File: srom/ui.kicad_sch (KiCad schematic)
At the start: 10 parts, among them J302 Conn_01x04_Female, J303 Conn_01x03_Female, J304 Conn_01x06_Female, SW301 SW_MEC_5E, SW302 RotaryEncoder_Switch, SW303 SW_MEC_5E, U301 Pico-3 UI

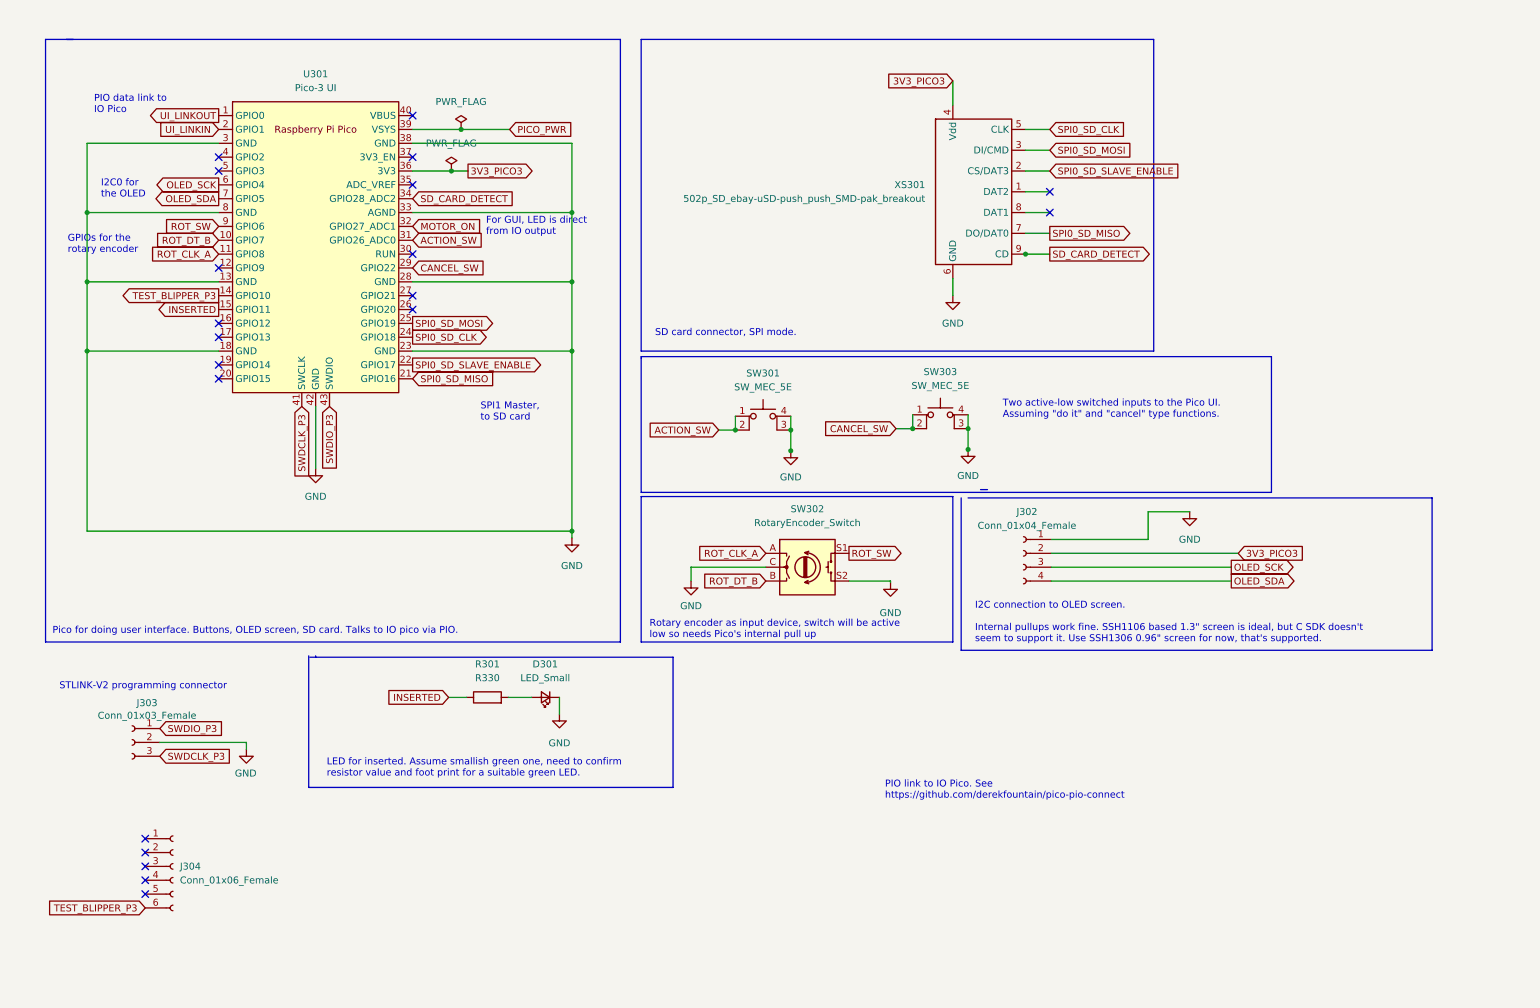
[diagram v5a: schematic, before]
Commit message: add rear edge schematic, RUN switch, ROMCS2 signal
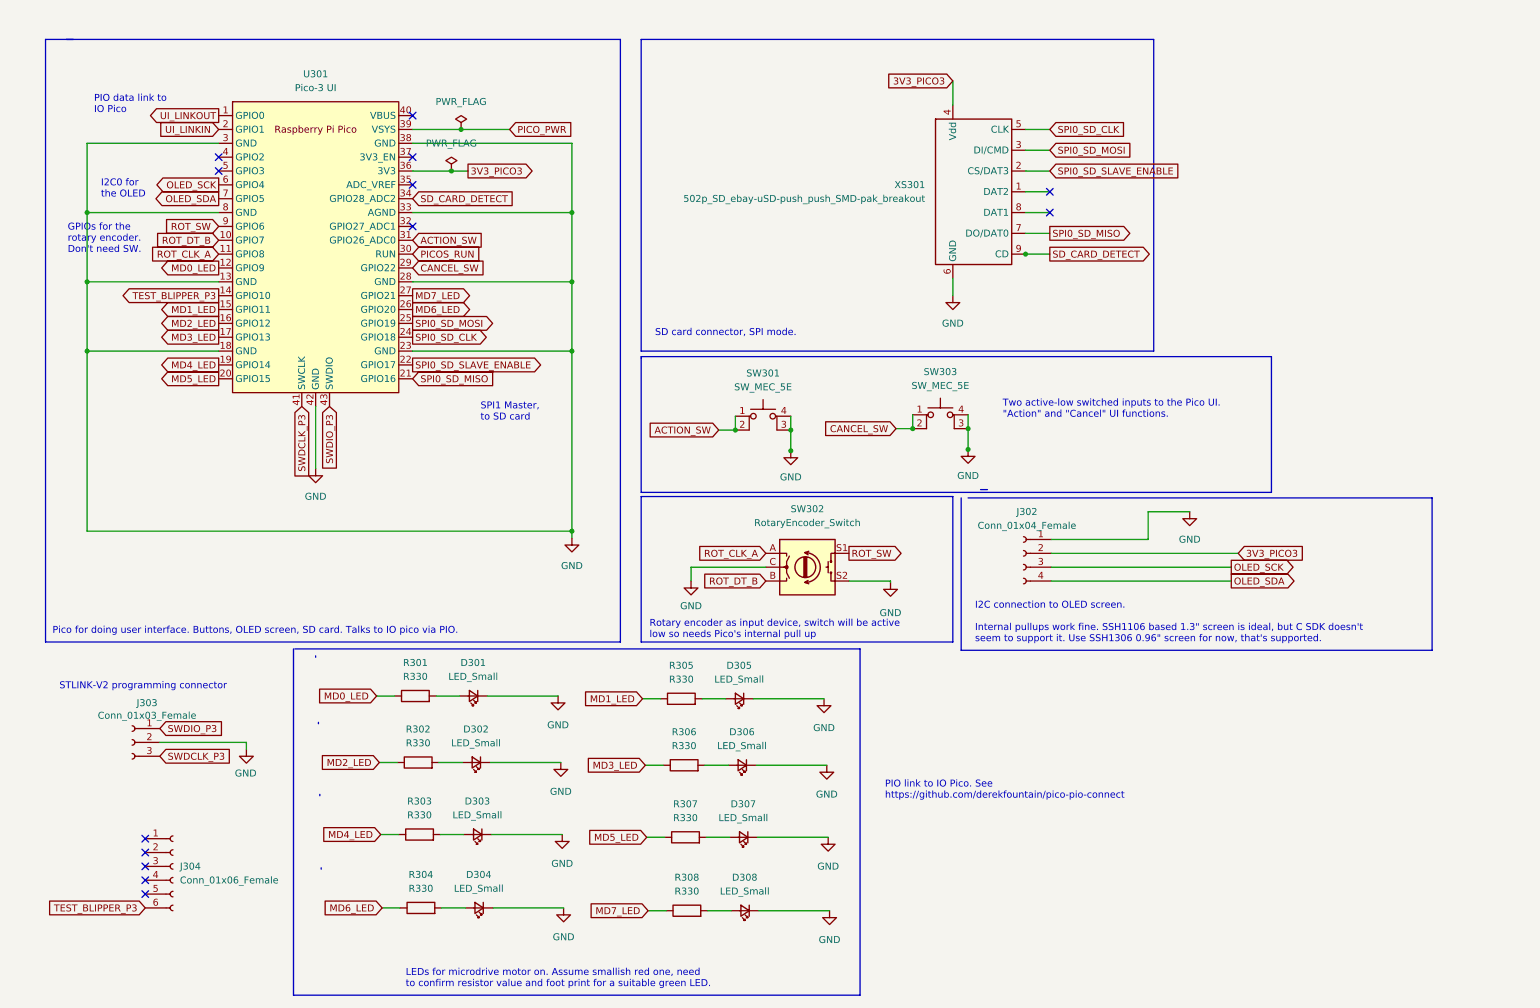
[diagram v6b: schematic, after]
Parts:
- added D302, D303, D304, D305, D306, D307, D308: LED_Small, LED_THT:LED_D3.0mm, symbol Device:LED_Small
- added R302, R303, R304, R305, R306, R307, R308: R330, Resistor_SMD:R_1206_3216Metric_Pad1.30x1.75mm_HandSolder, symbol Device:R
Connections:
- net GND: now also D302.1 (K), D303.1 (K), D304.1 (K), D305.1 (K), D306.1 (K), D307.1 (K), D308.1 (K)
- net MD0_LED: now reaches U301.12 (GPIO9)
- net MD0_LED: now also R301.1
- net MD2_LED: now reaches U301.16 (GPIO12)
- net MD2_LED: now also R302.1
- net MD3_LED: now reaches U301.17 (GPIO13)
- net MD3_LED: now also R306.1
- net MD4_LED: now reaches U301.19 (GPIO14)
- net MD4_LED: now also R303.1
- net MD5_LED: now reaches U301.20 (GPIO15)
- net MD5_LED: now also R307.1
- net MD6_LED: now reaches U301.26 (GPIO20)
- net MD6_LED: now also R304.1
- net MD7_LED: now reaches U301.27 (GPIO21)
- net MD7_LED: now also R308.1
- net PICOS_RUN: now reaches U301.30 (RUN)
- net INSERTED renamed MD1_LED
- net MD1_LED: now also R305.1; no longer R301.1
- net MOTOR_ON: no longer names the net of U301.32 (GPIO27_ADC1)
- new net: D304.2 (A), R304.2
- new net: D302.2 (A), R302.2
- new net: D308.2 (A), R308.2
- new net: D305.2 (A), R305.2
- new net: D303.2 (A), R303.2
- new net: D306.2 (A), R306.2
- new net: D307.2 (A), R307.2
- no-connect marks 20 -> 13
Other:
- note added: "GPIOs for the rotary encoder. Don't need SW."
- note added: "LEDs for microdrive motor on. Assume smallish red one, need to confirm resistor value and foot print for a suitable green LED."
- note added: "Two active-low switched inputs to the Pico UI. "Action" and "Cancel" UI functions."
- note removed: "For GUI, LED is direct from IO output"
- note removed: "GPIOs for the rotary encoder"
- note removed: "LED for inserted. Assume smallish green one, need to confirm resistor value and foot print for a suitable green LED."
- note removed: "Two active-low switched inputs to the Pico UI. Assuming "do it" and "cancel" type functions."
- moved on the sheet: D301, R301

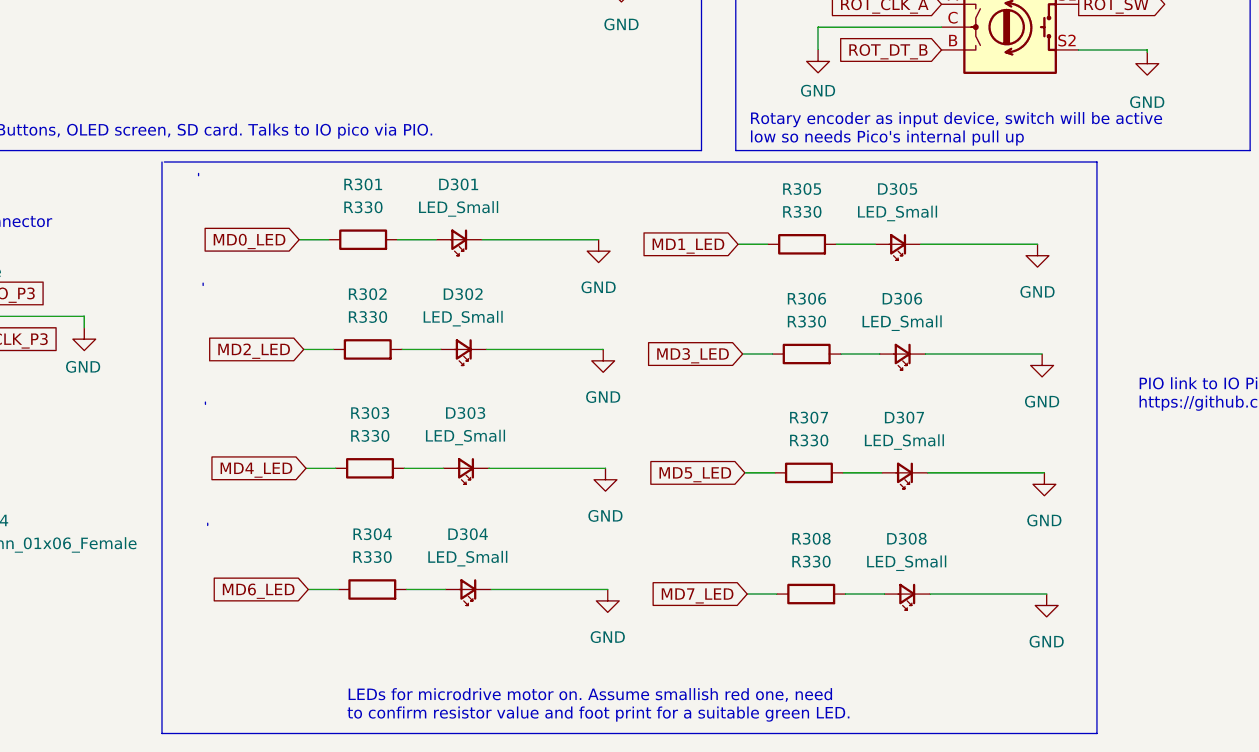
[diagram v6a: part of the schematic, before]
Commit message: 8 LEDs on UI Pico's GPIOs, 2 tested and working
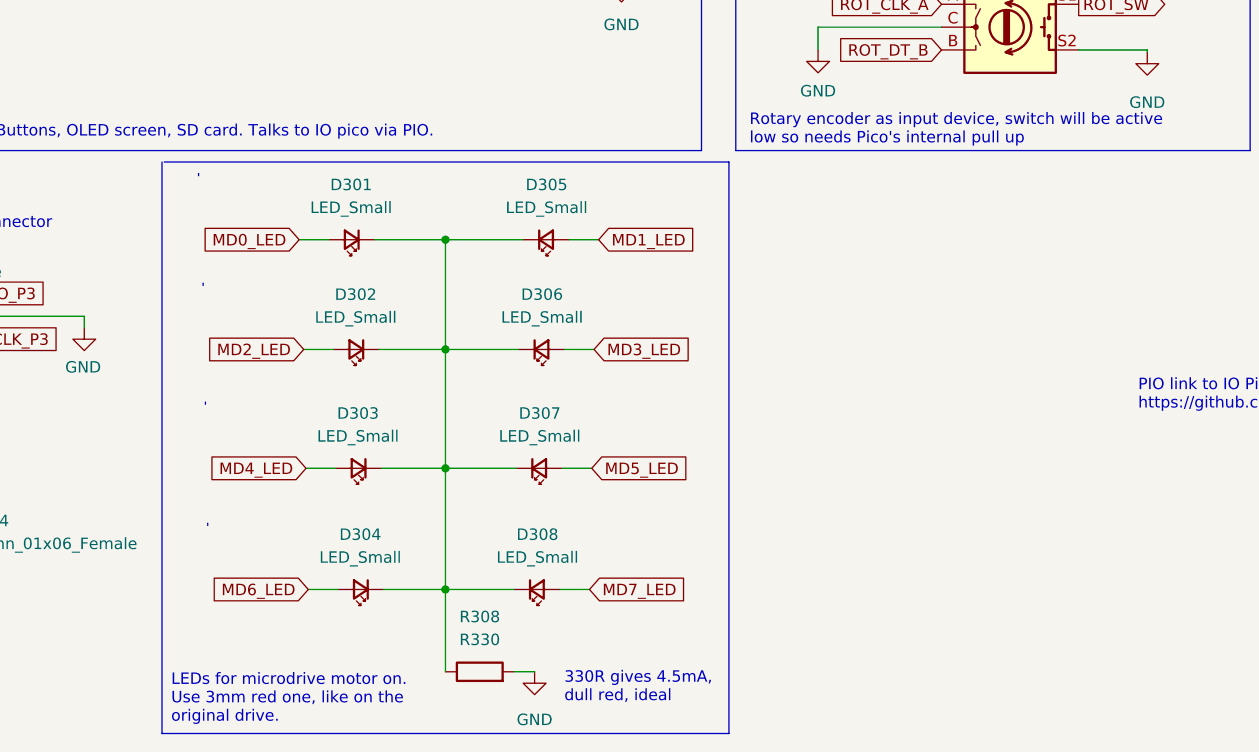
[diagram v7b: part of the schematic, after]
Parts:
- removed R301, R302, R303, R304, R305, R306, R307: R330, Resistor_SMD:R_1206_3216Metric_Pad1.30x1.75mm_HandSolder, symbol Device:R
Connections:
- net GND: now also R308.2; no longer D301.1 (K), D302.1 (K), D303.1 (K), D304.1 (K), D305.1 (K), D306.1 (K), D307.1 (K), D308.1 (K)
- net MD0_LED: now also D301.2 (A)
- net MD1_LED: now also D305.2 (A)
- net MD2_LED: now also D302.2 (A)
- net MD3_LED: now also D306.2 (A)
- net MD4_LED: now also D303.2 (A)
- net MD5_LED: now also D307.2 (A)
- net MD6_LED: now also D304.2 (A)
- net MD7_LED: now also D308.2 (A); no longer R308.1
- new net: D301.1 (K), D302.1 (K), D303.1 (K), D304.1 (K), D305.1 (K), D306.1 (K), D307.1 (K), D308.1 (K), R308.1
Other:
- note added: "330R gives 4.5mA, dull red, ideal"
- note added: "LEDs for microdrive motor on. Use 3mm red one, like on the original drive."
- note removed: "LEDs for microdrive motor on. Assume smallish red one, need to confirm resistor value and foot print for a suitable green LED."
- moved on the sheet: D301, D302, D303, D304, D305, D306, D307, D308, R308

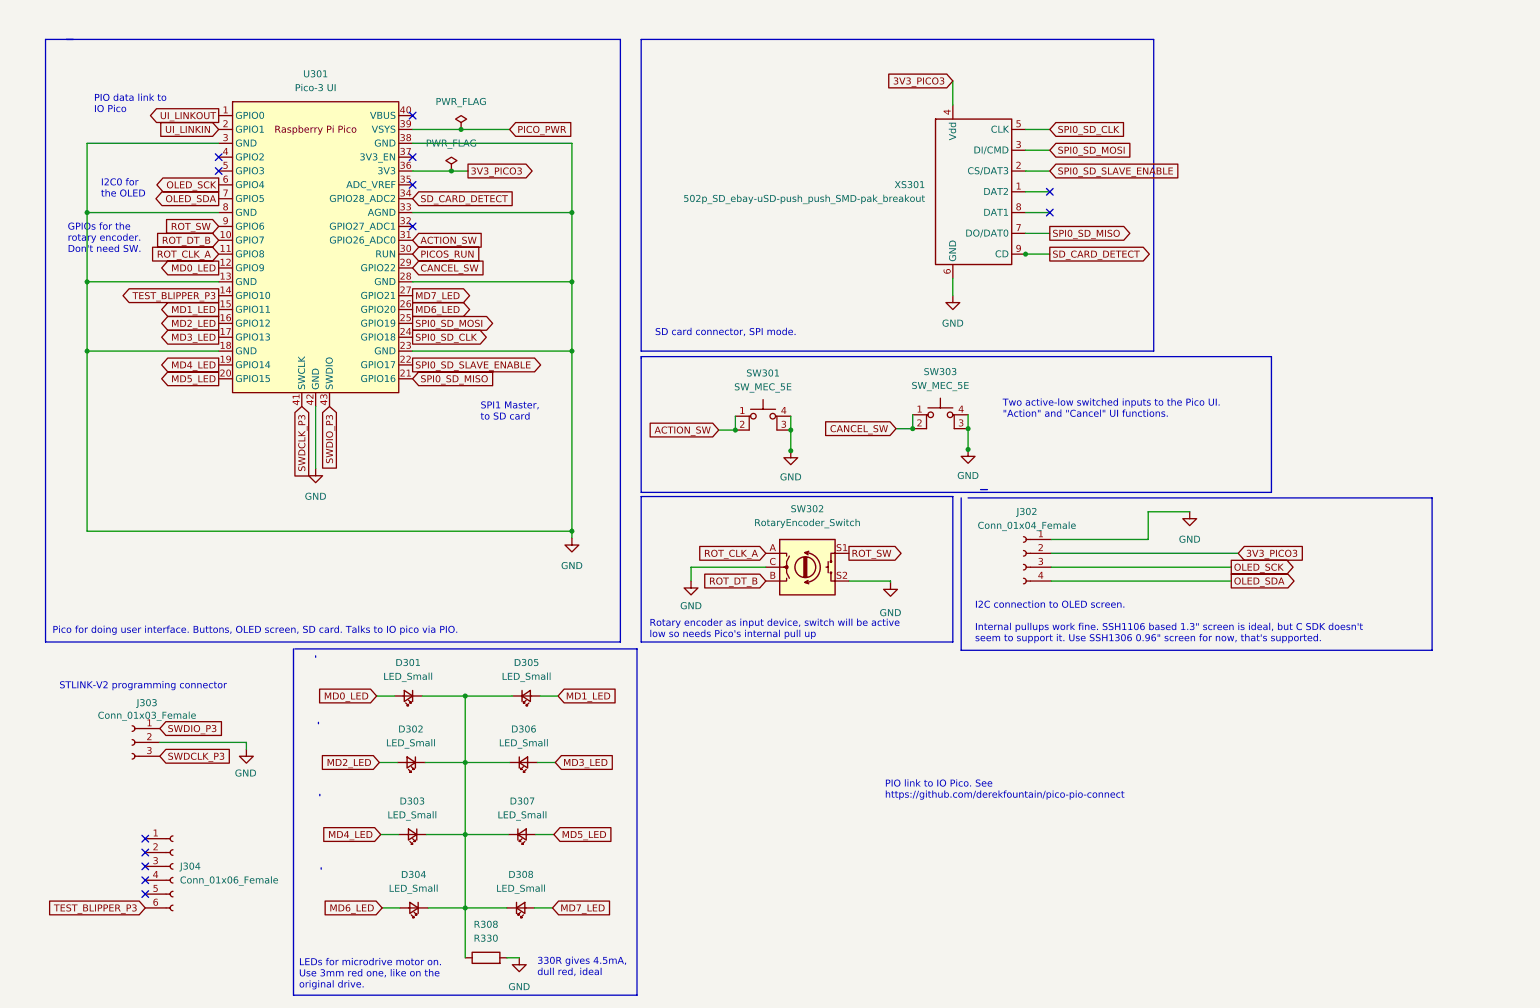
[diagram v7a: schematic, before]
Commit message: remove test point connectors, no needed on next board (famous last words)
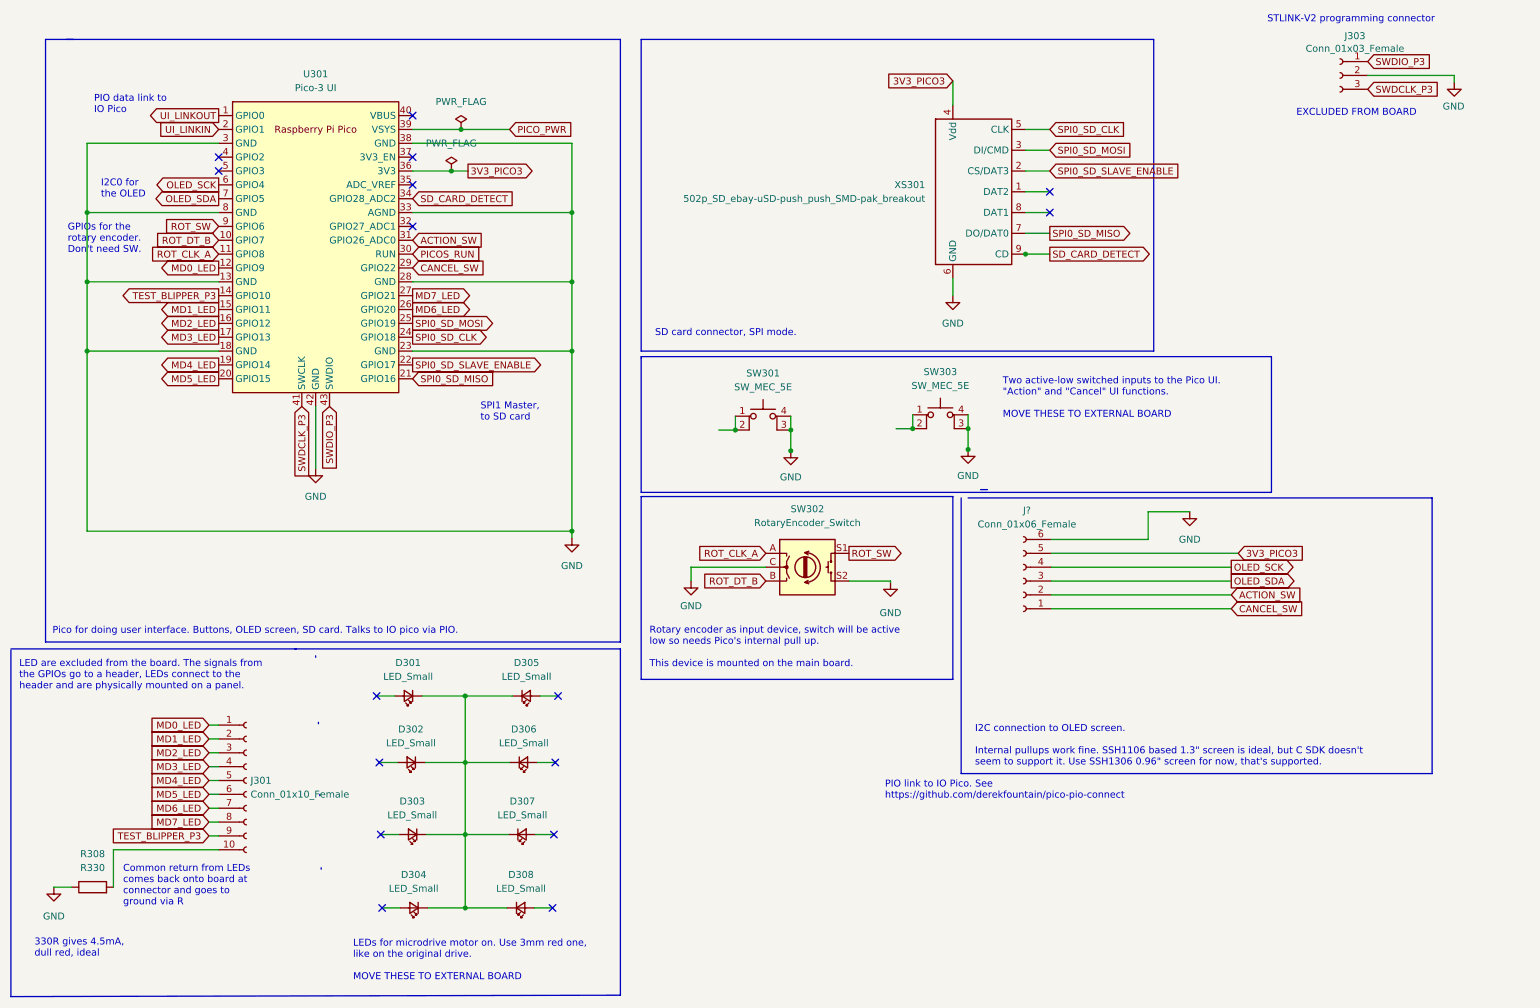
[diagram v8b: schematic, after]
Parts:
- removed J302: Conn_01x04_Female, Connector_PinHeader_2.54mm:PinHeader_1x04_P2.54mm_Vertical, symbol Connector:Conn_01x04_Female
- removed J304: Conn_01x06_Female, Connector_PinHeader_2.54mm:PinHeader_1x06_P2.54mm_Vertical, symbol Connector:Conn_01x06_Female
- added J301: Conn_01x10_Female, symbol Connector:Conn_01x10_Female
- added J?: Conn_01x06_Female, symbol Connector:Conn_01x06_Female
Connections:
- net 3V3_PICO3: now also J?.5 (Pin_5)
- net ACTION_SW: now also J?.2 (Pin_2); no longer SW301.1, SW301.2
- net CANCEL_SW: now also J?.1 (Pin_1); no longer SW303.1, SW303.2
- net GND: now also R308.1, J?.6 (Pin_6); no longer R308.2
- net MD0_LED: now also J301.1 (Pin_1); no longer D301.2 (A)
- net MD1_LED: now also J301.2 (Pin_2); no longer D305.2 (A)
- net MD2_LED: now also J301.3 (Pin_3); no longer D302.2 (A)
- net MD3_LED: now also J301.4 (Pin_4); no longer D306.2 (A)
- net MD4_LED: now also J301.5 (Pin_5); no longer D303.2 (A)
- net MD5_LED: now also J301.6 (Pin_6); no longer D307.2 (A)
- net MD6_LED: now also J301.7 (Pin_7); no longer D304.2 (A)
- net MD7_LED: now also J301.8 (Pin_8); no longer D308.2 (A)
- net OLED_SCK: now also J?.4 (Pin_4)
- net OLED_SDA: now also J?.3 (Pin_3)
- net TEST_BLIPPER_P3: now also J301.9 (Pin_9)
- net at D301.1 (K), D302.1 (K), D303.1 (K)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: no longer R308.1
- new net: SW301.1, SW301.2
- new net: J301.10 (Pin_10), R308.2
- new net: SW303.1, SW303.2
- no-connect marks 13 -> 16
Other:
- note added: "Common return from LEDs comes back onto board at connector and goes to ground via R"
- note added: "EXCLUDED FROM BOARD"
- note added: "LED are excluded from the board. The signals from the GPIOs go to a header, LEDs connect to the header and are physically mounted on a panel."
- note added: "LEDs for microdrive motor on. Use 3mm red one, like on the original drive. MOVE THESE TO EXTERNAL BOARD"
- note added: "Rotary encoder as input device, switch will be active low so needs Pico's internal pull up. This device is mounted on the main board."
- note added: "Two active-low switched inputs to the Pico UI. "Action" and "Cancel" UI functions. MOVE THESE TO EXTERNAL BOARD"
- note removed: "LEDs for microdrive motor on. Use 3mm red one, like on the original drive."
- note removed: "Rotary encoder as input device, switch will be active low so needs Pico's internal pull up"
- note removed: "Two active-low switched inputs to the Pico UI. "Action" and "Cancel" UI functions."
- moved on the sheet: J303, R308
